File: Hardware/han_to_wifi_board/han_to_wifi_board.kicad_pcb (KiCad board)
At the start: 2 copper layers, 36.8 x 57.8 mm, 38 parts, among them IC1 MIC2779L-2YM5_TR, J1 RJLSE4118101, J2 Conn_01x04_Male, SW1 RESET, U1 ESP-12F, U2 LT8619, U3 NCN5150

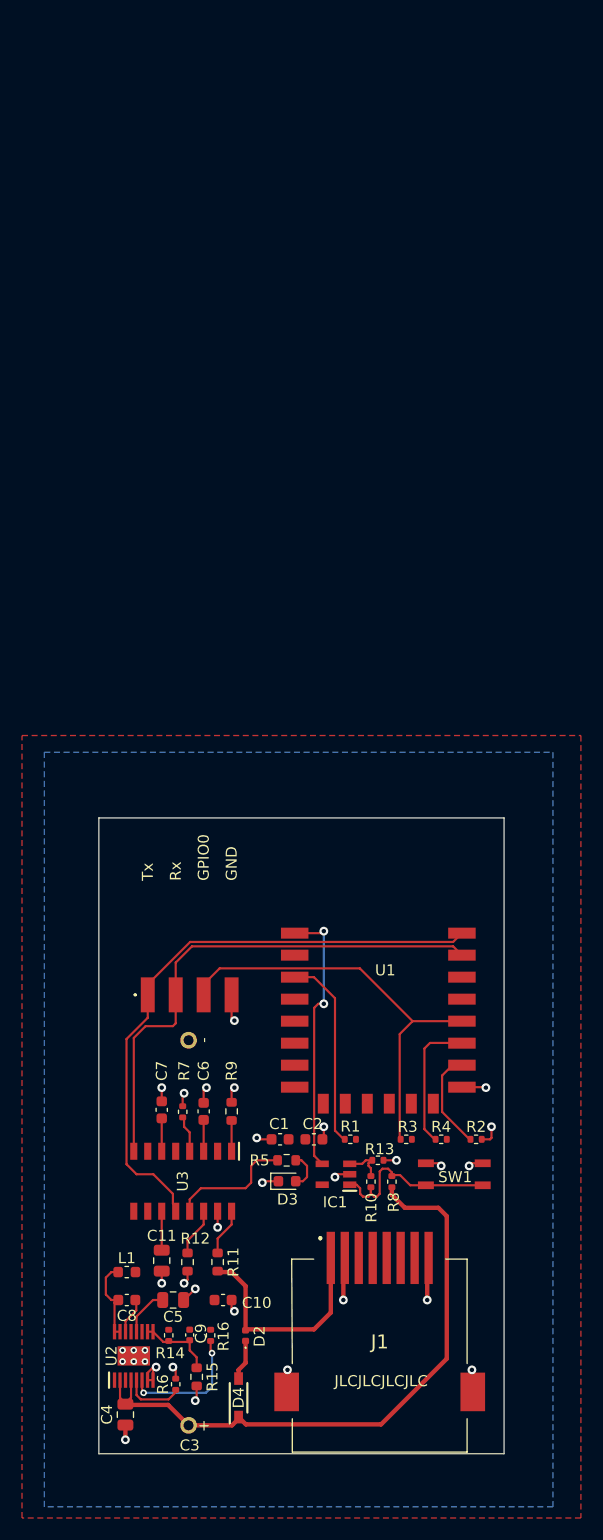
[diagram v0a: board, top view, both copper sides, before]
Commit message: New buck converter
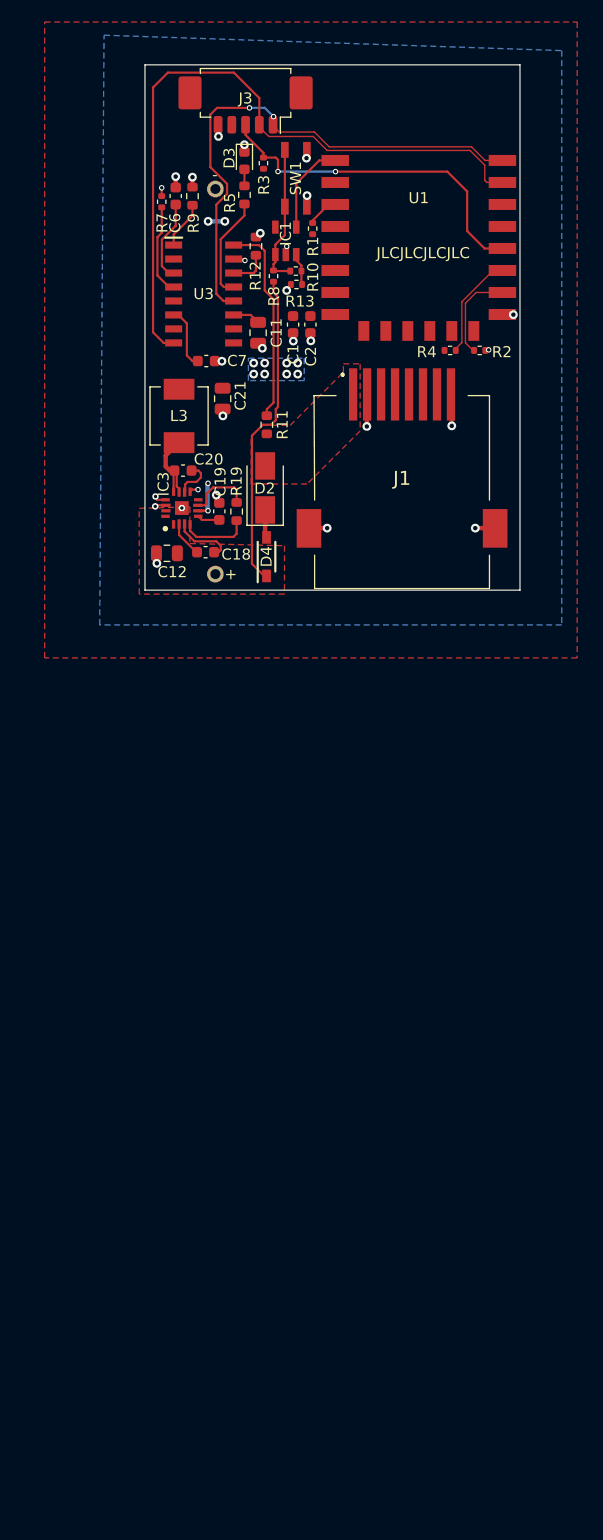
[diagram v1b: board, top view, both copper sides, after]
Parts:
- removed C10: 22µ, Capacitor_SMD:C_0603_1608Metric
- removed C4: 2.2µ, Capacitor_SMD:C_0805_2012Metric
- removed C5: 1µ, Capacitor_SMD:C_0805_2012Metric
- removed C8: 0.1µ, Capacitor_SMD:C_0603_1608Metric
- removed C9: 6.8p, Capacitor_SMD:C_0402_1005Metric
- removed J2: Conn_01x04_Male, TSM-104-02-S-SH-001:TSM10402SSH001
- removed L1: 15µH, Inductor_SMD:L_0603_1608Metric
- removed R14: 1M, Resistor_SMD:R_0402_1005Metric
- removed R15: 316k, Resistor_SMD:R_0603_1608Metric
- removed R16: 100k, Resistor_SMD:R_0402_1005Metric
- removed R6: 121k, Resistor_SMD:R_0402_1005Metric
- removed U2: LT8619, LIB_LT8619EMSE-5#PBF:SOP50P490X110-17N
- added C12: 4.7µF, Capacitor_SMD:C_0805_2012Metric, F.Cu at (117.3, 69.3)
- added C18: 2.2µF, Capacitor_SMD:C_0603_1608Metric, F.Cu at (120.8, 69.2)
- added C19: 5600pF, Capacitor_SMD:C_0603_1608Metric, F.Cu at (122.1, 65.5)
- added C20: 0.1µF, Capacitor_SMD:C_0603_1608Metric, F.Cu at (118.8, 61.8)
- added C21: 47µF, Capacitor_SMD:C_0805_2012Metric, F.Cu at (122.4, 55.2)
- added IC3: MAX17644AATE+, MAX17644AATE+:QFN50P300X300X80-17N, F.Cu at (118.7, 65.2)
- added J3: Conn_01x05_Male, Connector_Molex:Molex_PicoBlade_53261-0571_1x05-1MP_P1.25mm_Horizontal, F.Cu at (124.5, 27.9)
- added L3: 5.6µH, Inductor_SMD:L_Vishay_IHLP-2020, F.Cu at (118.4, 56.8)
- added R19: 40k2, Resistor_SMD:R_0603_1608Metric, F.Cu at (123.6, 65.5)
- D2: value D_Schottky_ALT -> 700mV, 2A; footprint Diode_SMD:D_0402_1005Metric -> Diode_SMD:D_SMA
- moved D3 92.8 mm to (124.4, 33.6), turned to -90 degrees
- moved R12 92.5 mm to (125.4, 41.4), turned to 90 degrees
- moved SW1 91.7 mm to (129.0, 35.2), turned to -90 degrees
- moved R3 89.7 mm to (126.1, 33.8), turned to 90 degrees
- moved R5 87.8 mm to (124.4, 36.7), turned to -90 degrees
- moved IC1 85.0 mm to (128.1, 40.9), turned to 90 degrees
- moved C11 84.8 mm to (125.6, 49.2)
- moved R9 83.3 mm to (119.6, 36.8)
- moved C6 83.2 mm to (118.1, 36.8)
- moved R10 83.0 mm to (129.0, 43.6), turned to 180 degrees
- moved R8 83.0 mm to (127.0, 44.1)
- moved R1 82.8 mm to (130.6, 39.8), turned to -90 degrees
- moved R7 82.7 mm to (116.8, 37.3)
- moved U3 80.7 mm to (120.7, 45.7), turned to 0 degrees
- moved R13 79.9 mm to (129.1, 44.9), turned to 0 degrees
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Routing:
- net GND: track 47.2 -> 15.5 mm, vias 33 -> 28
- net /24V: track 57.1 -> 29.0 mm
- net HAN1: track 20.3 -> 0.27 mm
- net /~{RST}: track 24.8 -> 8.37 mm, vias 2 -> 0
- net /ESP_Rx: track 47.1 -> 63.3 mm
- net Net-(R1-Pad1): track 17.6 -> 2.88 mm
- net Net-(R11-Pad1): track 4.23 -> 18.6 mm
- net Net-(R16-Pad2): track 11.8 -> 0.00 mm, vias 2 -> 0
- net Net-(C20-Pad1): track 0.00 -> 7.77 mm
- net Net-(C8-Pad2): track 7.59 -> 0.00 mm
- net /ESP_Tx: track 54.6 -> 47.7 mm, vias 0 -> 2
- net Net-(C9-Pad2): track 6.84 -> 0.00 mm
- net /GPIO0: track 38.2 -> 31.5 mm, vias 0 -> 2
- net Net-(IC3-Pad4): track 0.00 -> 6.38 mm
- net Net-(IC3-Pad7): track 0.00 -> 5.99 mm
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- added copper zone on B.Cu, net +3V3
- added copper zone on F.Cu, net /24V
- added copper zone on F.Cu, net HAN1
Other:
- board size 36.8 x 57.8 mm -> 34.1 x 47.8 mm
- board text added: "HAN-modul Nicholas Braaten Mai 2022"
- board text removed: "GND"
- board text removed: "GPIO0"
- board text removed: "HAN modul Nicholas Braaten Januar 2022"
- board text removed: "Rx"
- board text removed: "Tx"

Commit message: Connected SGND on buck to GND
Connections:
- C18 pad 1: Net-(C18-Pad1) -> GND
- IC3 pad 3: Net-(C18-Pad1) -> GND
- IC3 pad 4: Net-(IC3-Pad4) -> GND
- R19 pad 2: Net-(IC3-Pad4) -> GND
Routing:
- net GND: track 15.5 -> 27.5 mm, vias 28 -> 30
- net Net-(IC3-Pad4): track 6.38 -> 0.00 mm
- net Net-(C18-Pad1): track 5.58 -> 0.00 mm

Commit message: September hw changes
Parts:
- removed SW1: RESET, Button_Switch_SMD:SW_SPST_EVQP2
- added PRGRM: PRGRM, Button_Switch_SMD:SW_SPST_EVQP2, F.Cu at (117.6, 35.2)
- added RST: RESET, Button_Switch_SMD:SW_SPST_EVQP2, F.Cu at (128.9, 35.1)
- R1, R10, R13, R2, R3, R4, R7, R8: footprint Resistor_SMD:R_0402_1005Metric -> Resistor_SMD:R_0603_1608Metric
- moved C6 15.1 mm to (120.8, 51.7), turned to -90 degrees
- moved R9 15.1 mm to (122.4, 51.7), turned to -90 degrees
- moved R7 14.5 mm to (119.0, 51.7), turned to -90 degrees
- moved R1 13.5 mm to (138.6, 50.6), turned to 0 degrees
- moved R3 4.43 mm to (121.7, 33.5), turned to -90 degrees
- moved R8 4.42 mm to (127.0, 48.5), turned to 90 degrees
- moved C7 3.70 mm to (117.2, 51.7), turned to 90 degrees
- moved D2 1.44 mm to (127.6, 62.9)
- moved D4 1.25 mm to (127.6, 69.6)
- moved C11 1.23 mm to (125.1, 48.1)
- moved U3 1.03 mm to (120.1, 44.9)
- moved R12 0.84 mm to (125.0, 42.1)
- moved J1 0.81 mm to (139.5, 62.5)
- moved R13 0.74 mm to (128.5, 45.3)
- moved R4 0.70 mm to (142.4, 50.6)
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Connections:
- IC3 pad 8: unconnected-(IC3-Pad8) -> /~{RST}
- R13 pad 1: GND -> Net-(IC1-Pad1)
- R13 pad 2: Net-(IC1-Pad3) -> GND
- R8 pad 1: Net-(IC1-Pad1) -> /24V
- R8 pad 2: /24V -> Net-(IC1-Pad3)
- U1 pad 1: /~{RST} -> unconnected-(U1-Pad1)
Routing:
- net /~{RST}: track 8.37 -> 33.8 mm, vias 0 -> 2
- net Net-(R1-Pad1): track 2.88 -> 16.4 mm
- net /GPIO0: track 31.5 -> 42.6 mm, vias 2 -> 0
- net /ESP_Tx: track 47.7 -> 58.4 mm
- net /ESP_Rx: track 63.3 -> 53.2 mm
- net Net-(IC1-Pad1): track 12.9 -> 3.91 mm
- net Net-(R9-Pad1): track 4.33 -> 12.8 mm
- net GND: track 27.5 -> 34.7 mm, vias 30 -> 33
- net Net-(IC1-Pad3): track 2.93 -> 9.50 mm
- net /24V: track 29.0 -> 25.4 mm, vias 0 -> 2
- net +3V3: track 5.00 -> 8.05 mm, vias 12 -> 2
- net Net-(C6-Pad1): track 7.45 -> 9.64 mm
- net Net-(R11-Pad1): track 18.6 -> 20.0 mm, vias 0 -> 2
- net Net-(R12-Pad1): track 3.51 -> 2.16 mm
- net Net-(C7-Pad2): track 5.63 -> 4.89 mm
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- removed copper zone on B.Cu, net +3V3
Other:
- board size 34.1 x 47.8 mm -> 34 x 48 mm
- board text added: "AMS-utleser Nicholas Braaten September 2022"
- board text removed: "HAN-modul Nicholas Braaten Mai 2022"

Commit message: Changes after first bringup
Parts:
- removed PRGRM: PRGRM, Button_Switch_SMD:SW_SPST_EVQP2
- removed RST: RESET, Button_Switch_SMD:SW_SPST_EVQP2
- added SW1: RESET, EVQP2:EVQP2, F.Cu at (128.4, 35.6)
- added SW2: PRGRM, EVQP2:EVQP2, F.Cu at (118.0, 35.2)
- L3: footprint Inductor_SMD:L_Vishay_IHLP-2020 -> IHLP2020BZER5R6M11:L_Vishay_IHLP-2020
- moved R3 1.02 mm to (120.7, 33.5), turned to 90 degrees
- moved C18 0.95 mm to (121.6, 68.6)
- moved C12 0.81 mm to (118.0, 68.8), turned to 180 degrees
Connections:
- IC3 pad 4: GND -> unconnected-(IC3-Pad4)
- IC3 pad 8: /~{RST} -> unconnected-(IC3-Pad8)
- R1 pad 1: Net-(R1-Pad1) -> /~{RST}
- U1 pad 3: Net-(R1-Pad1) -> /~{RST}
- U3 pad 13: /~{HAN} -> unconnected-(U3-Pad13)
- U3 pad 7: unconnected-(U3-Pad7) -> /~{HAN}
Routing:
- net /~{RST}: track 33.8 -> 53.1 mm
- net Net-(R1-Pad1): track 16.4 -> 0.00 mm
- net /~{HAN}: track 10.1 -> 18.8 mm
- net GND: track 34.7 -> 28.5 mm, vias 33 -> 32
- net +3V3: track 8.05 -> 4.84 mm
- net /GPIO0: track 42.6 -> 39.7 mm
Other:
- outline, holes or cut-outs redrawn
- board text added: "PRGRM"
- board text added: "RST"
